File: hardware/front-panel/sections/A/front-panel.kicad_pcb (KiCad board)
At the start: 4 copper layers, 180 x 100 mm, 76 parts, among them J1 Conn_02x20_Odd_Even, J10 SMA, J11 SMA, J12 SMA, J13 SMA, J14 SMA, J15 SMA, J16 SMA, J17 SMA, J18 SMA, J19 SMA, J2 Conn_02x20_Odd_Even, J20 SMA, J21 SMA, J22 SMA, J23 SMA, J24 SMA, J25 SMA, J3 Conn_02x20_Odd_Even, J30 OLED 0.96in module on 1x4 soc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, J31 KF128-2.54-10P, J32 KF128-5.0-2P, J33 Qwiic (vertical), J40 Module header 2x6 (shrouded), J411 KF301-5.0-2P, J412 KF301-5.0-2P, Q411 MMBT5551, Q412 MMBT5551, Q421 MMBT5551, Q422 MMBT5551, U401 6N137S-TA1-L, U402 6N137S-TA1-L, U410 SN74AHCT541PWR

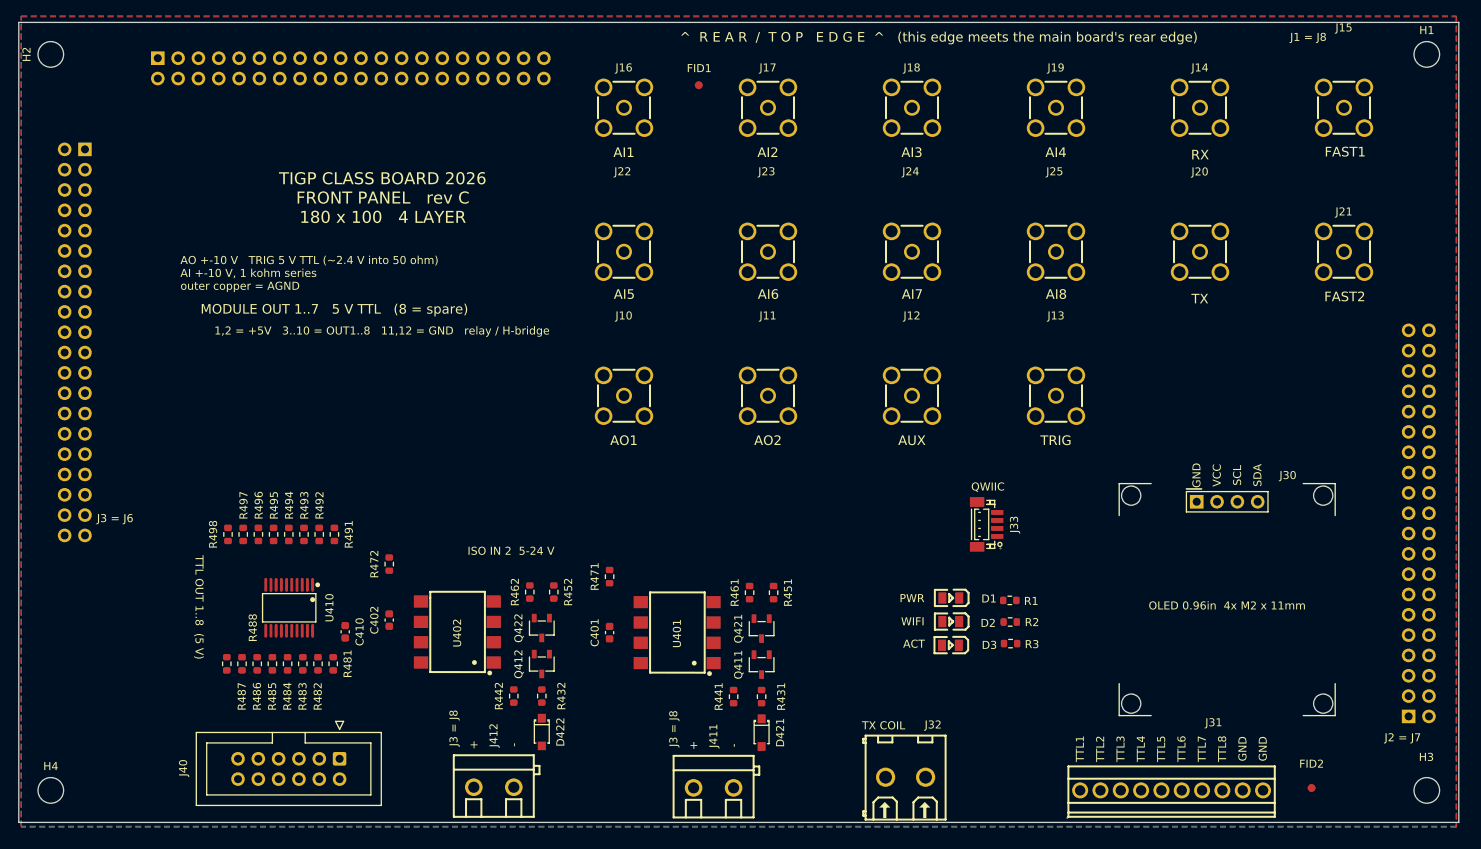
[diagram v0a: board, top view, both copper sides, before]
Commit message: front panel section A: route the 13 analog nets
DRC on hardware/front-panel/sections/A/front-panel.kicad_pcb: 0 unconnected
items and 0 clearance violations on all 13 of section A's nets (AI1-AI8, AO1,
AO2, AUX, RX, TX). 90 tracks, 77 on F.Cu and 13 on B.Cu, no vias. No footprint
moved, no zone changed, no track on an inner layer, and no track on a net that
belongs to another section.

Notes on the two that needed thought:

- TX at J20: the direct diagonal came within 0.062 mm of J20's AGND pad against
  a 0.2 mm rule, so that corner goes round as an L instead. TX also occupies two
  pins of the link header (J1 pads 20 and 22), which needed a short link between
  them, and a duplicated 34 mm parallel run plus several spur ends were removed.

- AUX is the only net on B.Cu. Its run from J1 pad 12 to J13 pad 5 is about
  107 mm and F.Cu is taken up by the SMA field and the other analog nets, so it
  crosses on the back. No via is needed: both J1 and J13 are through-hole pads,
  so a B.Cu track lands on them directly.

Remaining DRC warnings are not this section's: 3 lib_footprint_mismatch
(library drift on the instructor's footprints), 2 silk_over_copper, and 1
track_dangling at a T-junction whose connection is real - removing that track
breaks TX's connectivity.

Co-Authored-By: Claude Opus 5 (1M context) <noreply@anthropic.com>
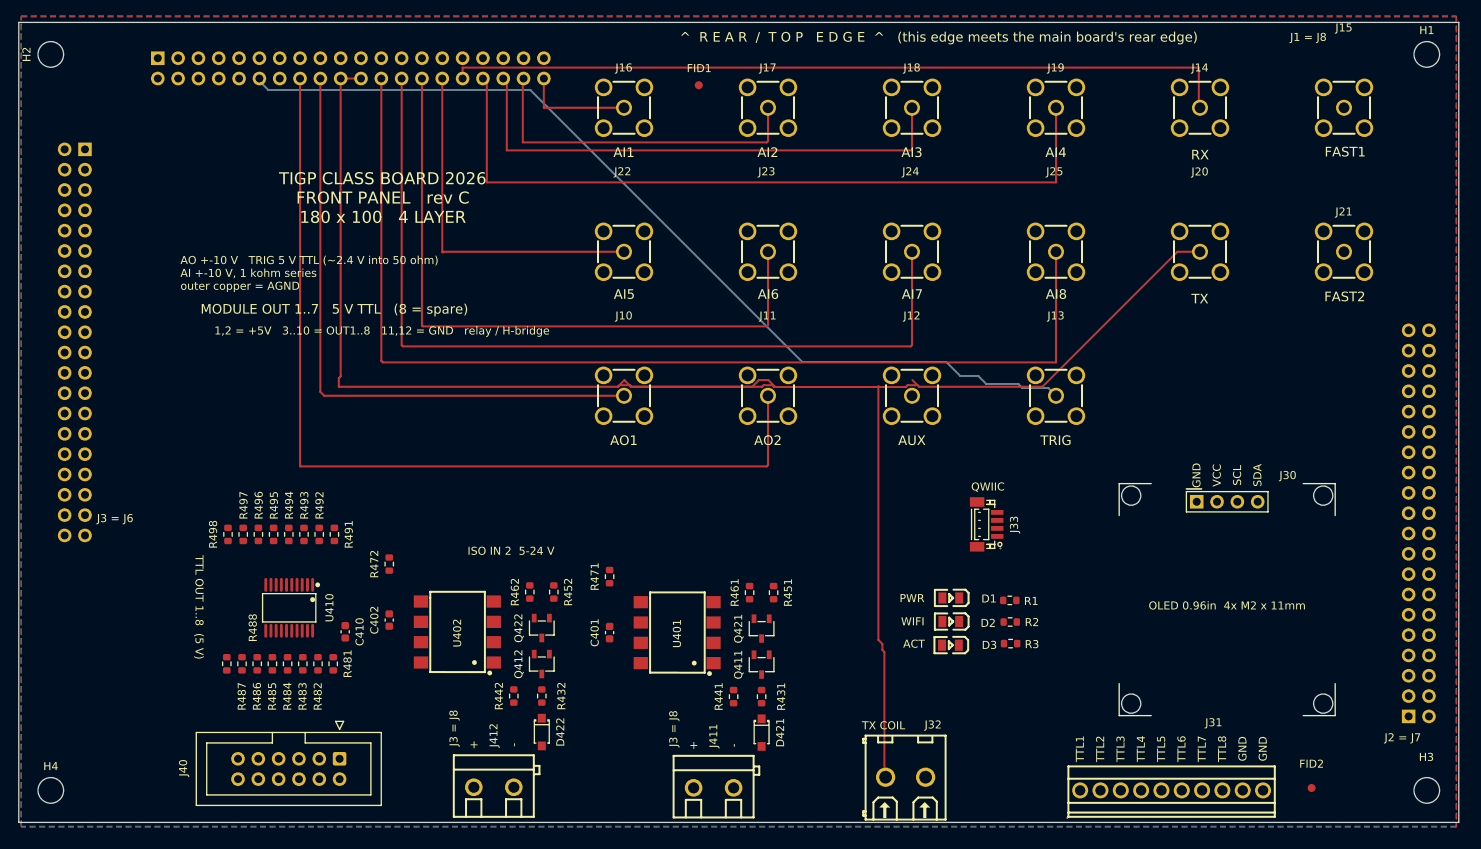
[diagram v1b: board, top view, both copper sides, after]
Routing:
- net /TX: track 0.00 -> 226.3 mm
- net /AI8: track 0.00 -> 133.5 mm
- net /AUX: track 0.00 -> 116.2 mm
- net /AO2: track 0.00 -> 115.7 mm
- net /AI7: track 0.00 -> 108.9 mm
- net /RX: track 0.00 -> 98.5 mm
- net /AI4: track 0.00 -> 94.2 mm
- net /AI6: track 0.00 -> 83.4 mm
- net /AO1: track 0.00 -> 77.3 mm
- net /AI3: track 0.00 -> 65.1 mm
- net /AI5: track 0.00 -> 44.4 mm
- net /AI2: track 0.00 -> 42.9 mm
- net /AI1: track 0.00 -> 13.7 mm

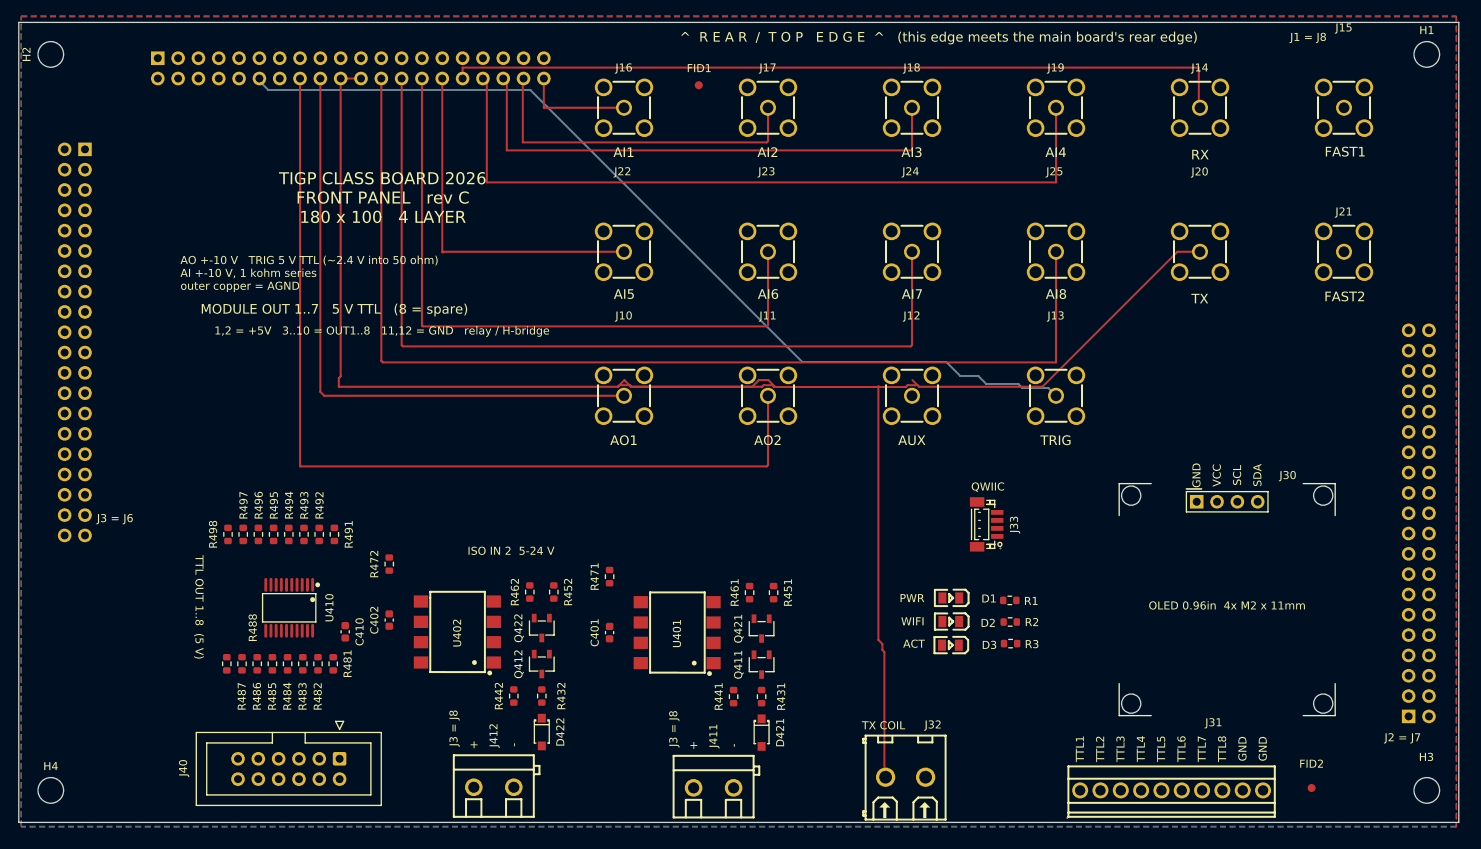
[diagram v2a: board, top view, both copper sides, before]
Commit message: Main board: five copper zones restored (missing from the 2026-09-24 save), student A's area-A routing accepted (26 items; 157 unconnected); Decision #70: three students on the boards (A Renqian, B Yi-Tsai, C instructor, D Lihdong) in both sections READMEs; sections re-split
Co-Authored-By: Claude Fable 5.1 <noreply@anthropic.com>
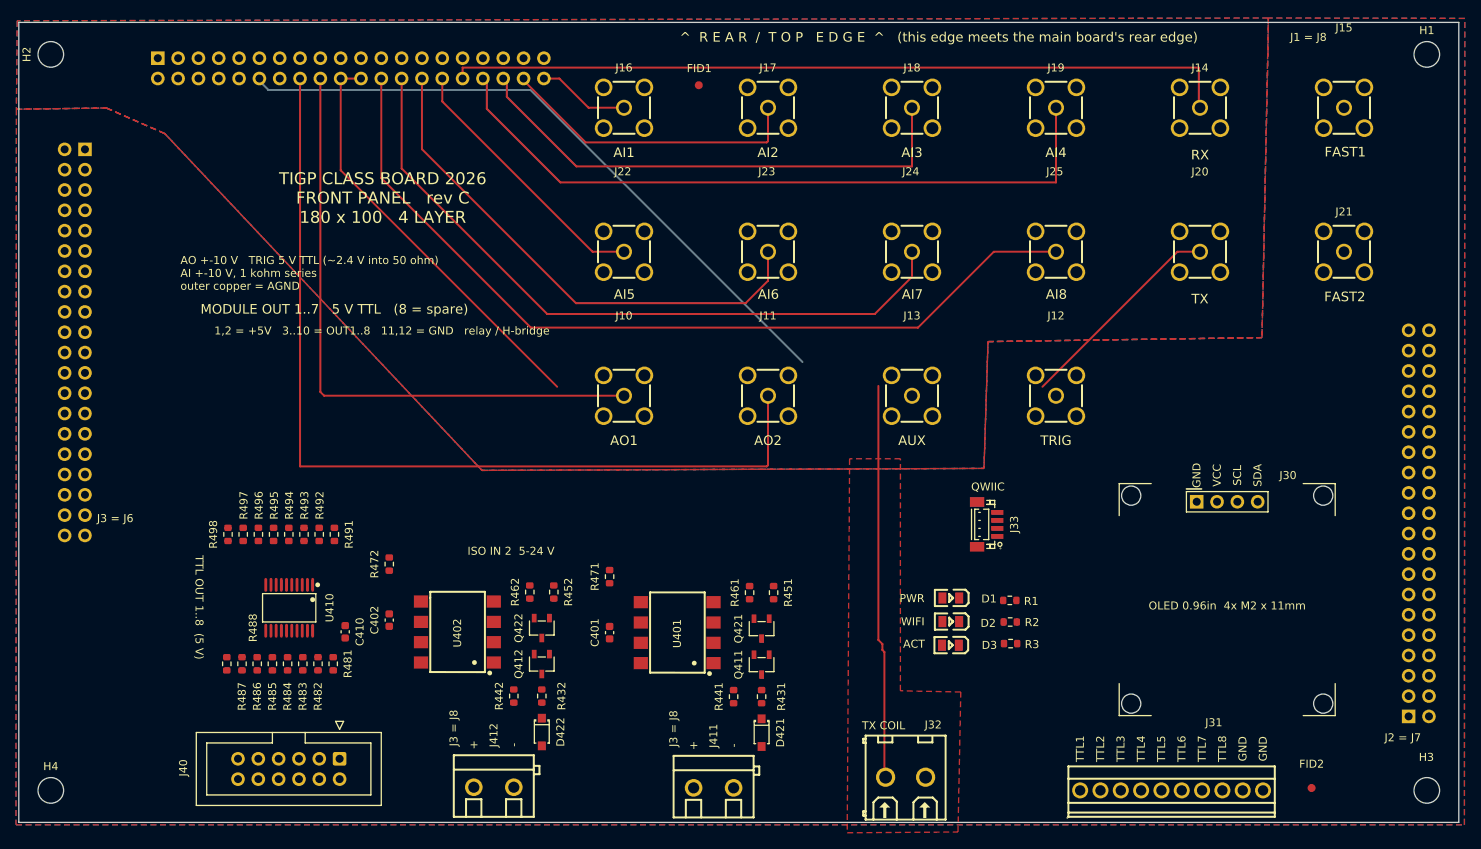
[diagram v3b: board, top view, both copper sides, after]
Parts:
- moved J12 18.0 mm to (129.7, 61.7)
- moved J13 18.0 mm to (111.7, 61.7)
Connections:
- J12 pad 1: AGND -> GND
- J12 pad 2: AGND -> GND
- J12 pad 3: AGND -> GND
- J12 pad 4: AGND -> GND
- J14 pad 5: /RX -> /TX
- J15 pad 1: AGND -> GND
- J15 pad 2: AGND -> GND
- J15 pad 3: AGND -> GND
- J15 pad 4: AGND -> GND
- J20 pad 5: /TX -> /RX
- J21 pad 1: AGND -> GND
- J21 pad 2: AGND -> GND
- J21 pad 3: AGND -> GND
- J21 pad 4: AGND -> GND
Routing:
- net /TX: track 226.3 -> 100.3 mm
- net /AUX: track 116.2 -> 82.7 mm
- net /RX: track 98.5 -> 125.1 mm
- net /AI8: track 133.5 -> 108.5 mm
- net /AI7: track 108.9 -> 87.6 mm
- net /AI6: track 83.4 -> 64.9 mm
- net /AI5: track 44.4 -> 33.4 mm
- net /AI4: track 94.2 -> 88.8 mm
- net /AI2: track 42.9 -> 38.3 mm
- net /AI1: track 13.7 -> 11.5 mm
- net /AI3: track 65.1 -> 64.1 mm
- added copper zone on B.Cu, net AGND
- added copper zone on In2.Cu, net AGND
- added copper zone on F.Cu, net GND
- added copper zone on In1.Cu, net GND

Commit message: hardware: panel master with students A/B section routing accepted, from repo main c3a4043
Co-Authored-By: Claude Fable 5.1 <noreply@anthropic.com>
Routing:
- net GND: track 0.00 -> 242.2 mm, vias 0 -> 1
- net /AUX: track 82.7 -> 254.7 mm
- net /TTL1: track 0.00 -> 67.6 mm
- net /TTL2: track 0.00 -> 62.3 mm
- net /TTL3: track 0.00 -> 57.8 mm
- net /TTL4: track 0.00 -> 52.2 mm
- net /TTL5: track 0.00 -> 47.2 mm
- net /TTL6: track 0.00 -> 42.0 mm
- net /TTL7: track 0.00 -> 36.8 mm
- net /FASTTTL1: track 0.00 -> 35.6 mm
- net /TTL8: track 0.00 -> 31.8 mm
- net /FASTTTL2: track 0.00 -> 20.2 mm
- net /LED_ACT_A: track 0.00 -> 5.73 mm
- net /LED_PWR_A: track 0.00 -> 5.62 mm
- net /LED_WIFI_A: track 0.00 -> 5.57 mm

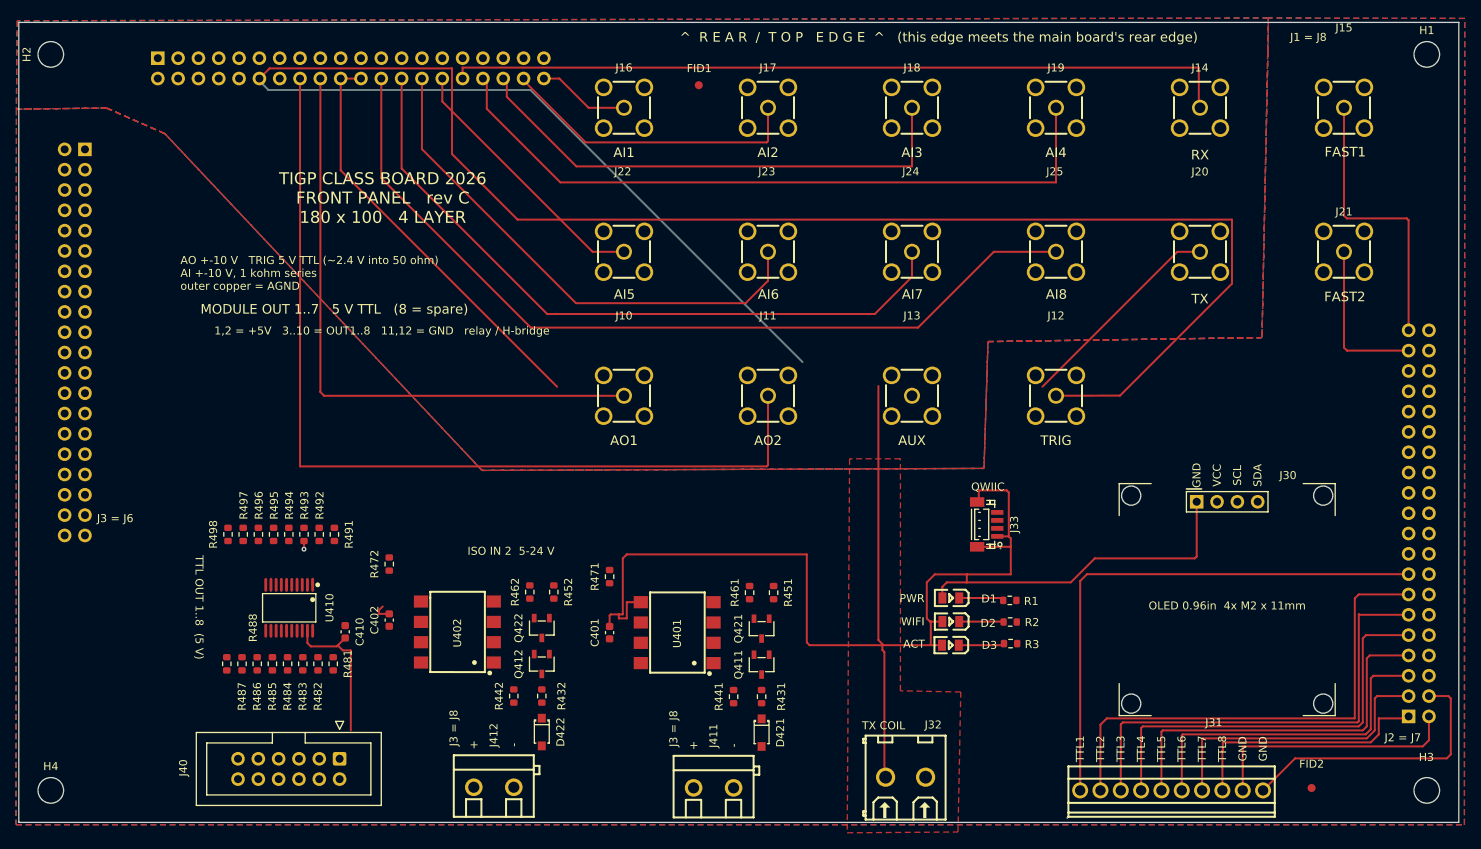
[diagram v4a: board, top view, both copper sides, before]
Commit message: hardware: sections re-split, from repo main c485506
Co-Authored-By: Claude Fable 5.1 <noreply@anthropic.com>
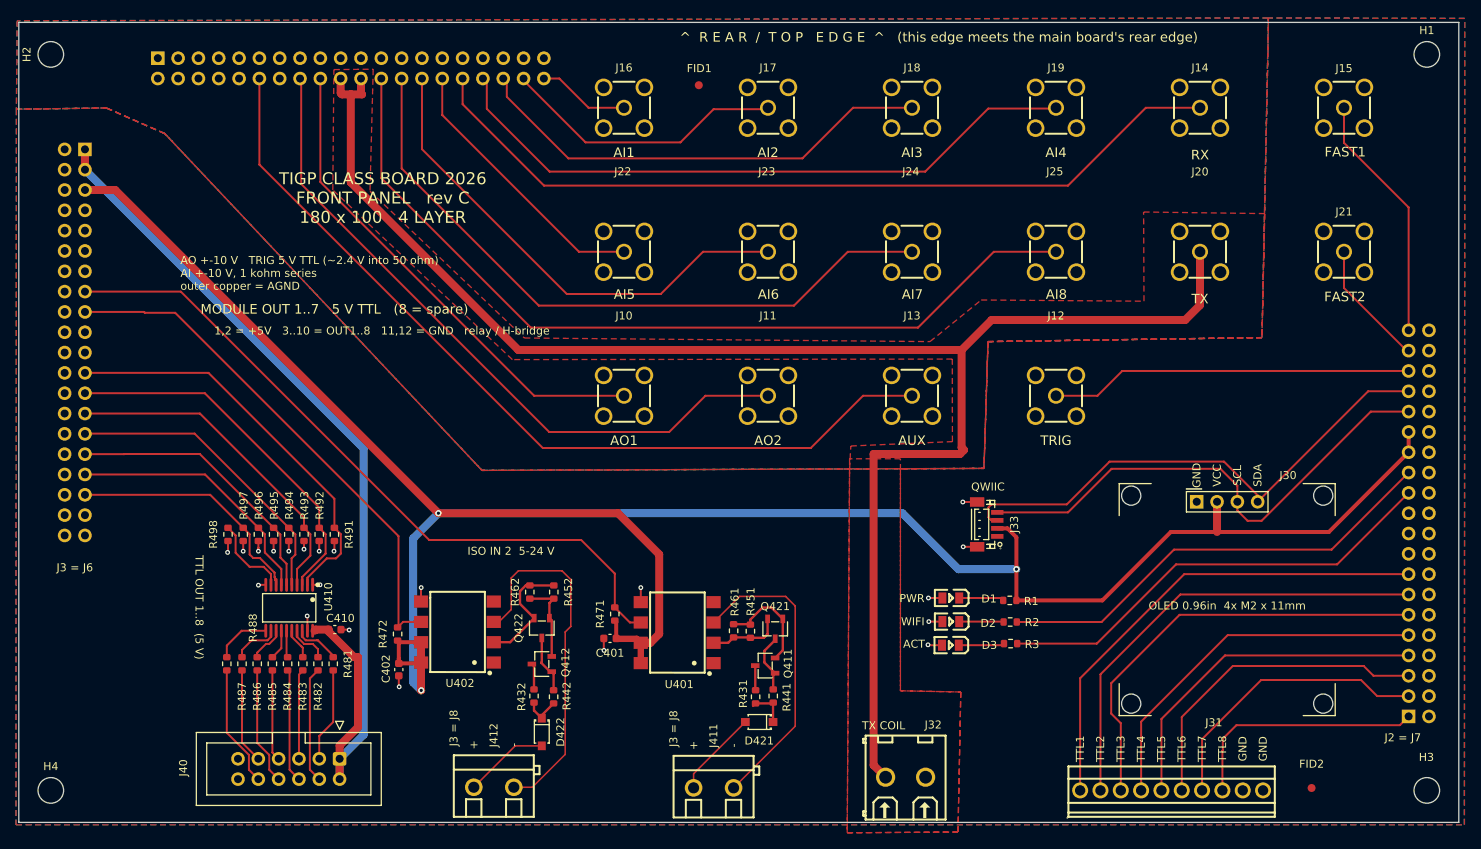
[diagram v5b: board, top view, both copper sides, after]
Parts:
- moved R472 8.80 mm to (47.4, 91.5)
- moved C402 6.30 mm to (47.5, 95.9), turned to -90 degrees
- moved R451 5.63 mm to (91.5, 91.1), turned to -90 degrees
- moved R461 5.17 mm to (89.3, 91.0), turned to -90 degrees
- moved R442 4.98 mm to (66.8, 99.3)
- moved R441 4.95 mm to (94.3, 99.2)
- moved R471 4.72 mm to (74.5, 89.0)
- moved Q421 1.70 mm to (94.5, 90.8)
- moved D421 1.36 mm to (92.5, 102.5), turned to 180 degrees
- moved C410 1.33 mm to (39.5, 90.9), turned to 0 degrees
- moved R432 0.98 mm to (64.4, 99.2)
- moved R431 0.75 mm to (92.1, 99.3)
- moved C401 0.72 mm to (73.9, 92.0), turned to 180 degrees
- moved Q411 0.47 mm to (93.3, 95.4), turned to 0 degrees
- turned Q412 to 0 degrees
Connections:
- J14 pad 5: /TX -> /RX
- J20 pad 5: /RX -> /TX
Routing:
- net +3V3: track 0.00 -> 299.0 mm, vias 0 -> 3
- net GND: track 242.2 -> 32.1 mm, vias 1 -> 21
- net /AUX: track 254.7 -> 110.0 mm
- net +5V_RAW: track 0.00 -> 120.2 mm
- net /TX: track 100.3 -> 206.6 mm
- net /OPTO_IN1: track 0.00 -> 89.1 mm
- net /I2C_SDA: track 0.00 -> 65.7 mm
- net /OPTO_IN2: track 0.00 -> 65.5 mm
- net /I2C_SCL: track 0.00 -> 63.8 mm
- net /LED_ACT: track 0.00 -> 56.7 mm
- net /LED_WIFI: track 0.00 -> 56.7 mm
- net /MOD1: track 0.00 -> 51.2 mm
- net /MOD2: track 0.00 -> 46.4 mm
- net /TRIG_5V: track 0.00 -> 45.4 mm
- net /ISO2_IN-: track 0.00 -> 45.3 mm
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- added copper zone on F.Cu, net /TX
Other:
- board text removed: "J1 = J8"
- board text removed: "J1 J2 J3 mate J6 J7 J8 of the main board; pin 1 marked"
- board text removed: "J1 pin 1"
- board text removed: "J1 pin 40"
- board text removed: "J2 pin 1"
- board text removed: "J2 pin 40"
